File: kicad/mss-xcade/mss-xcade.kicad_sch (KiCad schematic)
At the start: 52 parts, among them J1 Screw_Terminal_01x02, J2 SM04B-SRSS, J3 690-005-299-043, J4 SM04B-SRSS, J5 Conn_02x03_Odd_Even, J6 SM04B-SRSS, SW1 FSM4JSMATR, SW2 SW_DIP_x08, U1 AZ1117-3.3, U2 AP63205WU, U3 PCA9546ADR, U4 ESP32-S2-SOLO

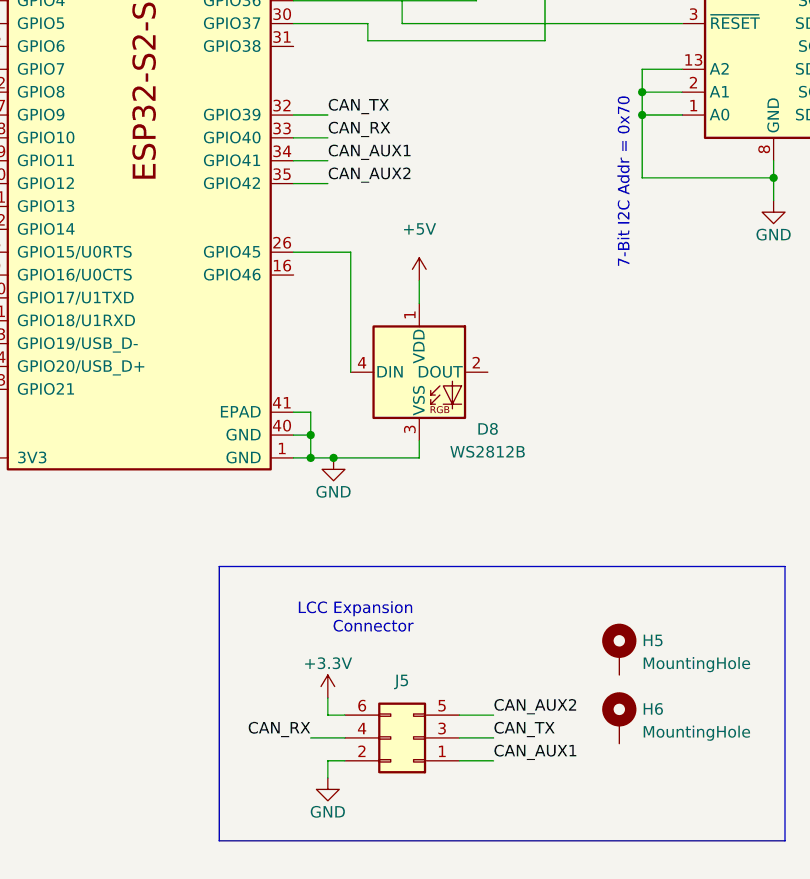
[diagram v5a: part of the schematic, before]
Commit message: Update expansion connector and add CAN interface module board
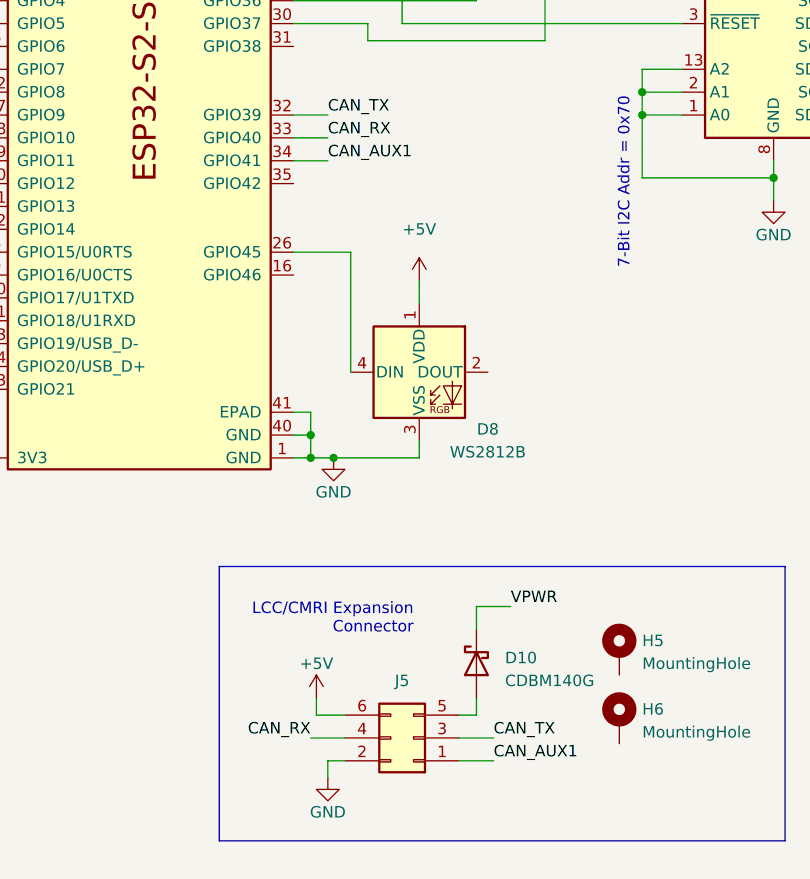
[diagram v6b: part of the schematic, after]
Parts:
- added D10: CDBM140G, ISE_Generic:SOD-123T, symbol Device:D_Schottky
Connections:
- net +3.3V: no longer J5.6 (Pin_6)
- net +5V: now also J5.6 (Pin_6)
- net VPWR: now also D10.1 (K)
- net CAN_AUX2: no longer names the net of U4.35 (GPIO42)
- net CAN_AUX2: no longer J5.5 (Pin_5)
- new net: D10.2 (A), J5.5 (Pin_5)
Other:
- note added: "LCC/CMRI Expansion Connector"
- note removed: "LCC Expansion Connector"
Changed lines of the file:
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@@
-    (stroke (width 0) (type default) (color 0 0 0 0))
-  )
-  (wire (pts (xy 107.315 177.165) (xy 107.315 175.26))
     (stroke (width 0) (type default) (color 0 0 0 0))
   )
@@
     (stroke (width 0) (type default) (color 0 0 0 0))
   )
-  (wire (pts (xy 109.22 177.165) (xy 107.315 177.165))
-    (stroke (width 0) (type default) (color 0 0 0 0))
-  )
   (wire (pts (xy 275.59 106.68) (xy 275.59 109.22))
     (stroke (width 0) (type default) (color 0 0 0 0))
@@
     (stroke (width 0) (type default) (color 0 0 0 0))
   )
+  (wire (pts (xy 121.92 177.165) (xy 123.825 177.165))
+    (stroke (width 0) (type default) (color 0 0 0 0))
+  )
   (wire (pts (xy 146.685 29.21) (xy 146.685 27.94))
     (stroke (width 0) (type default) (color 0 0 0 0))
@@
     (stroke (width 0) (type default) (color 0 0 0 0))
   )
+  (wire (pts (xy 123.825 167.64) (xy 123.825 165.1))
+    (stroke (width 0) (type default) (color 0 0 0 0))
+  )
   (wire (pts (xy 103.505 113.03) (xy 107.315 113.03))
     (stroke (width 0) (type default) (color 0 0 0 0))
@@
     (stroke (width 0) (type default) (color 0 0 0 0))
   )
-  (wire (pts (xy 125.73 177.165) (xy 121.92 177.165))
-    (stroke (width 0) (type default) (color 0 0 0 0))
-  )
   (wire (pts (xy 201.295 43.18) (xy 201.295 48.26))
     (stroke (width 0) (type default) (color 0 0 0 0))
@@
     (stroke (width 0) (type default) (color 0 0 0 0))
   )
+  (wire (pts (xy 123.825 177.165) (xy 123.825 175.26))
+    (stroke (width 0) (type default) (color 0 0 0 0))
+  )
   (wire (pts (xy 275.59 119.38) (xy 275.59 121.92))
     (stroke (width 0) (type default) (color 0 0 0 0))
@@
     (stroke (width 0) (type default) (color 0 0 0 0))
   )
+  (wire (pts (xy 123.825 165.1) (xy 127.635 165.1))
+    (stroke (width 0) (type default) (color 0 0 0 0))
+  )
   (wire (pts (xy 108.585 33.02) (xy 141.605 33.02))
     (stroke (width 0) (type default) (color 0 0 0 0))
@@
     (stroke (width 0) (type default) (color 0 0 0 0))
   )
-  (wire (pts (xy 103.505 118.11) (xy 107.315 118.11))
-    (stroke (width 0) (type default) (color 0 0 0 0))
-  )
   (wire (pts (xy 166.37 43.18) (xy 166.37 48.26))
     (stroke (width 0) (type default) (color 0 0 0 0))
@@
     (stroke (width 0) (type default) (color 0 0 0 0))
   )
+  (wire (pts (xy 106.045 175.26) (xy 106.045 177.165))
+    (stroke (width 0) (type default) (color 0 0 0 0))
+  )
   (polyline (pts (xy 100.965 160.655) (xy 158.115 160.655))
     (stroke (width 0) (type default) (color 0 0 0 0))
@@
     (stroke (width 0) (type default) (color 0 0 0 0))
   )
+  (wire (pts (xy 106.045 177.165) (xy 109.22 177.165))
+    (stroke (width 0) (type default) (color 0 0 0 0))
+  )
   (wire (pts (xy 103.505 148.59) (xy 105.41 148.59))
     (stroke (width 0) (type default) (color 0 0 0 0))
@@
     (stroke (width 0) (type default) (color 0 0 0 0))
   )
-  (text "LCC Expansion\nConnector" (at 116.84 168.275 180)
+  (text "LCC/CMRI Expansion\nConnector" (at 116.84 168.275 180)
     (effects (font (size 1.27 1.27)) (justify right bottom))
   )
@@
     (effects (font (size 1.27 1.27)) (justify left bottom))
   )
-  (label "CAN_AUX2" (at 107.315 118.11 0)
-    (effects (font (size 1.27 1.27)) (justify left bottom))
-  )
   (label "CAN_TX" (at 107.315 110.49 0)
     (effects (font (size 1.27 1.27)) (justify left bottom))
@@
   )
   (label "CONF_SW2" (at 247.65 106.68 0)
-    (effects (font (size 1.27 1.27)) (justify left bottom))
-  )
-  (label "CAN_AUX2" (at 125.73 177.165 0)
     (effects (font (size 1.27 1.27)) (justify left bottom))
   )
@@
   )
   (label "CONF_SW8" (at 56.515 110.49 0)
+    (effects (font (size 1.27 1.27)) (justify left bottom))
+  )
+  (label "VPWR" (at 127.635 165.1 0)
     (effects (font (size 1.27 1.27)) (justify left bottom))
   )
@@
     (pin "1")
   )
+  (symbol (lib_id "power:+5V") (at 106.045 175.26 0) (unit 1)
+    (in_bom yes) (on_board yes)
+    (property "Reference" "#PWR025" (id 0) (at 106.045 179.07 0)
+      (effects (font (size 1.27 1.27)) hide)
+    )
+    (property "Value" "+5V" (id 1) (at 106.045 171.45 0))
+    (property "Footprint" "" (id 2) (at 106.045 175.26 0)
+      (effects (font (size 1.27 1.27)) hide)
+    )
+    (property "Datasheet" "" (id 3) (at 106.045 175.26 0)
+      (effects (font (size 1.27 1.27)) hide)
+    )
+    (pin "1")
+  )
   (symbol (lib_id "Connector_Generic:Conn_02x03_Odd_Even") (at 116.84 179.705 180) (unit 1)
     (in_bom yes) (on_board yes)
@@
     (pin "2")
   )
-  (symbol (lib_id "power:+3.3V") (at 107.315 175.26 0) (unit 1)
-    (in_bom yes) (on_board yes)
-    (property "Reference" "#PWR0113" (id 0) (at 107.315 179.07 0)
-      (effects (font (size 1.27 1.27)) hide)
-    )
-    (property "Value" "+3.3V" (id 1) (at 107.315 171.45 0))
-    (property "Footprint" "" (id 2) (at 107.315 175.26 0)
-      (effects (font (size 1.27 1.27)) hide)
-    )
-    (property "Datasheet" "" (id 3) (at 107.315 175.26 0)
-      (effects (font (size 1.27 1.27)) hide)
-    )
-    (pin "1")
-  )
   (symbol (lib_id "Connector:TestPoint") (at 35.56 30.48 0) (mirror x) (unit 1)
     (in_bom yes) (on_board yes)
@@
     (pin "2")
   )
+  (symbol (lib_id "Device:D_Schottky") (at 123.825 171.45 90) (mirror x) (unit 1)
+    (in_bom yes) (on_board yes)
+    (property "Reference" "D10" (id 0) (at 127 170.815 90)
+      (effects (font (size 1.27 1.27)) (justify right))
+    )
+    (property "Value" "CDBM140G" (id 1) (at 127 173.355 90)
+      (effects (font (size 1.27 1.27)) (justify right))
+    )
+    (property "Footprint" "ISE_Generic:SOD-123T" (id 2) (at 123.825 171.45 0)
+      (effects (font (size 1.27 1.27)) hide)
+    )
+    (property "Datasheet" "~" (id 3) (at 123.825 171.45 0)
+      (effects (font (size 1.27 1.27)) hide)
+    )
+    (pin "1")
+    (pin "2")
+  )
   (symbol (lib_id "Connector:Screw_Terminal_01x02") (at 28.575 27.94 0) (mirror y) (unit 1)
     (in_bom yes) (on_board yes)
@@
       (reference "#PWR024") (unit 1) (value "GND") (footprint "")
     )
+    (path "/938d6c62-f864-44b0-ade5-3a5f95ffc68f"
+      (reference "#PWR025") (unit 1) (value "+5V") (footprint "")
+    )
     (path "/e1082014-b244-475d-b8a4-e8dc8b3e642a"
       (reference "#PWR027") (unit 1) (value "GND") (footprint "")
@@
       (reference "#PWR0112") (unit 1) (value "GND") (footprint "")
     )
-    (path "/dba43e29-17da-4a44-a819-2ab55386ea21"
-      (reference "#PWR0113") (unit 1) (value "+3.3V") (footprint "")
-    )
     (path "/3df14ada-ef8c-4faa-b2f5-b1b7df2998e6"
       (reference "#PWR0114") (unit 1) (value "+5V") (footprint "")
@@
       (reference "D9") (unit 1) (value "CDBM140G") (footprint "ISE_Generic:SOD-123T")
     )
+    (path "/f5d6a7cc-6656-4bea-b067-7e4438ecbb4d"
+      (reference "D10") (unit 1) (value "CDBM140G") (footprint "ISE_Generic:SOD-123T")
+    )
     (path "/fedd826e-74ae-4512-8096-f38aaffedb7c"
